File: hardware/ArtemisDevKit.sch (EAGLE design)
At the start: 79 parts, among them J2 CORTEX_JTAG_DEBUG_MINIMUM_PTH, J3 CORTEX_JTAG_DEBUG_PTH, J5 1X04_SMD_STRAIGHT_COMBO, J6 QWIIC_RIGHT_ANGLE, J7 CAMERA-HIMAX, J9 1X04_SMD_STRAIGHT_COMBO, U1 DAPLINK_KL26Z, U2 ARTEMIS_MODULESMD, U3 LIS2DH12, U4 AP2127K-1.8V, X1 16MHz, Y1 32.768kHz

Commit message: apply changes from proto review
- labeled jumpers w/ matching names and description
- labeled accelerometer axes (bottom)
- increaded power trace widths to 24 mil
- removed VUSB current limiting resistor
- increased buzzard label sizes
- added AP2112K 3.3V regulator (disconnected MKL26Z regulator output from 3.3V bus to avoid contention)
- added product name on top silk
- changed reset button to the tall smd version
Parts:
- removed JP1: JUMPER-SMT_2_NC_TRACE_SILK, SparkFun-Jumpers:JUMPER-SMT_2_NC_TRACE_SILK
- removed R17: 10, SparkFun-Resistors:10OHM-0603-1/10W-1%
- removed TP11, TP3, TP4: TEST-POINT3X5, SparkFun-Connectors:TEST-POINT3X5
- added TGT_BOOT: JUMPER-SMT_2_NC_TRACE_SILK, SparkFun-Jumpers:JUMPER-SMT_2_NC_TRACE_SILK
- added U5: 3.3V, SparkFun-IC-Power:V_REG_AP2112K-3.3V
- S2: device SparkFun-Switches:MOMENTARY-SWITCH-SPST-SMD-4.6X2.8MM -> SparkFun-Switches:MOMENTARY-SWITCH-SPST-SMD-5.2MM-TALL
- renumbered JP2 to TGT_SWD_CLK
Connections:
- removed net VBUS_IF: D6.5, J1.VBUS, J12.3, J12.4, J4.3, J4.4, J8.3, J8.4, R17.1
- removed net VBUS_IF2: C12.1, C13.1, R17.2, R19.2, U1.VREGIN
- new net V_USB: C12.1, C13.1, D6.5, J1.VBUS, J12.3, J12.4, J4.3, J4.4, J8.3, J8.4, R19.2, U1.VREGIN, U5.EN, U5.IN
- net !TGT_RST: no longer TP11.1
- net 3.3V: now also U5.OUT; no longer U1.VOUT33
- net GND: now also U5.GND
- net N$18: now also TGT_BOOT.1; no longer JP1.1
- net TGT_BOOT: now also TGT_BOOT.2; no longer JP1.2
- net TGT_RX: no longer TP4.1
- net TGT_TX: no longer TP3.1
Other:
- note added: "Cut to isolate Artemis boot pin from interface chip"
- note added: "Cut to isolate Artemis swd clock from interface chip"

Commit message: update to use MKL26Z128VFM4 from SparkFun library
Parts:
- U1: value DAPLINK_KL26Z -> DAPLINK_KL26Z128VFM4; device ArtemisDevKit:DAPLINK_KL26Z -> SparkFun-IC-Microcontroller:DAPLINK_KL26Z128VFM4

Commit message: update eagle libraries in brd + sch
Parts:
- J12, J8: device SparkFun-Connectors:CONN_08NO_SILK_FEMALE_PTH -> SparkFun-Connectors:CONN_08NO_SILK_DNP
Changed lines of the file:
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@@
 <part name="SUPPLY22" library="SparkFun-PowerSymbols" deviceset="3.3V" device=""/>
 <part name="J4" library="SparkFun-Connectors" deviceset="CONN_08" device="SMD-COMBO-FEMALE"/>
-<part name="J8" library="SparkFun-Connectors" deviceset="CONN_08" device="NO_SILK_FEMALE_PTH"/>
-<part name="J12" library="SparkFun-Connectors" deviceset="CONN_08" device="NO_SILK_FEMALE_PTH"/>
+<part name="J8" library="SparkFun-Connectors" deviceset="CONN_08" device="NO_SILK_DNP"/>
+<part name="J12" library="SparkFun-Connectors" deviceset="CONN_08" device="NO_SILK_DNP"/>
 <part name="SUPPLY5" library="SparkFun-PowerSymbols" deviceset="1.8V" device=""/>
 <part name="J14" library="SparkFun-Connectors" deviceset="CONN_12" device="NO_SILK"/>

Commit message: replace sparkfun logo in schematic
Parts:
- added LOGO2: SFE_LOGO_NAME_FLAME.2_INCH, SparkFun-Aesthetics:SFE_LOGO_NAME_FLAME.2_INCH

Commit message: QC double check changes
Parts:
- J1: value (none) -> USB
- J10, J11: value (none) -> SMD
- J14, J22, J23, J24, J25, J26: value (none) -> PTH
- J5, J9: value 1X04_SMD_STRAIGHT_COMBO -> SMD
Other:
- note added: "power rail intended for output only"
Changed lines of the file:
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@@
 <part name="C4" library="SparkFun-Capacitors" deviceset="0.1UF" device="-0603-25V-5%" value="0.1uF"/>
 <part name="R12" library="SparkFun-Resistors" deviceset="10KOHM" device="-0603-1/10W-1%" value="10k"/>
-<part name="J1" library="SparkFun-Connectors" deviceset="USB_C" device="_2-LAYER"/>
+<part name="J1" library="SparkFun-Connectors" deviceset="USB_C" device="_2-LAYER" value="USB"/>
 <part name="R6" library="SparkFun-Resistors" deviceset="5.1KOHM" device="5.1KOHM-0603-1/10W-1%" value="5.1k"/>
 <part name="R7" library="SparkFun-Resistors" deviceset="5.1KOHM" device="5.1KOHM-0603-1/10W-1%" value="5.1k"/>
@@
 <part name="J12" library="SparkFun-Connectors" deviceset="CONN_08" device="NO_SILK_DNP"/>
 <part name="SUPPLY5" library="SparkFun-PowerSymbols" deviceset="1.8V" device=""/>
-<part name="J14" library="SparkFun-Connectors" deviceset="CONN_12" device="NO_SILK"/>
-<part name="J22" library="SparkFun-Connectors" deviceset="CONN_12" device="NO_SILK"/>
-<part name="J23" library="SparkFun-Connectors" deviceset="CONN_12" device="NO_SILK"/>
-<part name="J24" library="SparkFun-Connectors" deviceset="CONN_12" device="NO_SILK"/>
-<part name="J25" library="SparkFun-Connectors" deviceset="CONN_12" device="NO_SILK"/>
-<part name="J26" library="SparkFun-Connectors" deviceset="CONN_12" device="NO_SILK"/>
+<part name="J14" library="SparkFun-Connectors" deviceset="CONN_12" device="NO_SILK" value="PTH"/>
+<part name="J22" library="SparkFun-Connectors" deviceset="CONN_12" device="NO_SILK" value="PTH"/>
+<part name="J23" library="SparkFun-Connectors" deviceset="CONN_12" device="NO_SILK" value="PTH"/>
+<part name="J24" library="SparkFun-Connectors" deviceset="CONN_12" device="NO_SILK" value="PTH"/>
+<part name="J25" library="SparkFun-Connectors" deviceset="CONN_12" device="NO_SILK" value="PTH"/>
+<part name="J26" library="SparkFun-Connectors" deviceset="CONN_12" device="NO_SILK" value="PTH"/>
 <part name="GND1" library="SparkFun-PowerSymbols" deviceset="GND" device=""/>
-<part name="J5" library="SparkFun-Connectors" deviceset="CONN_04" device="SMD_STRAIGHT_COMBO" value="1X04_SMD_STRAIGHT_COMBO"/>
-<part name="J9" library="SparkFun-Connectors" deviceset="CONN_04" device="SMD_STRAIGHT_COMBO" value="1X04_SMD_STRAIGHT_COMBO"/>
-<part name="J10" library="SparkFun-Connectors" deviceset="CONN_08" device="SMD-COMBO-FEMALE"/>
-<part name="J11" library="SparkFun-Connectors" deviceset="CONN_08" device="SMD-COMBO-FEMALE"/>
+<part name="J5" library="SparkFun-Connectors" deviceset="CONN_04" device="SMD_STRAIGHT_COMBO" value="SMD"/>
+<part name="J9" library="SparkFun-Connectors" deviceset="CONN_04" device="SMD_STRAIGHT_COMBO" value="SMD"/>
+<part name="J10" library="SparkFun-Connectors" deviceset="CONN_08" device="SMD-COMBO-FEMALE" value="SMD"/>
+<part name="J11" library="SparkFun-Connectors" deviceset="CONN_08" device="SMD-COMBO-FEMALE" value="SMD"/>
 <part name="GND23" library="SparkFun-PowerSymbols" deviceset="GND" device=""/>
 <part name="TGT_BOOT" library="SparkFun-Jumpers" deviceset="JUMPER-SMT_2_NC_TRACE" device="_SILK" package3d_urn="urn:adsk.eagle:package:39281/1"/>
@@
 <text x="116.84" y="203.2" size="1.27" layer="97" font="vector">Cut to isolate Artemis swd
 clock  from interface chip</text>
+<text x="363.22" y="180.34" size="1.778" layer="97" font="vector">power rail intended for output only</text>
 </plain>
 <instances>

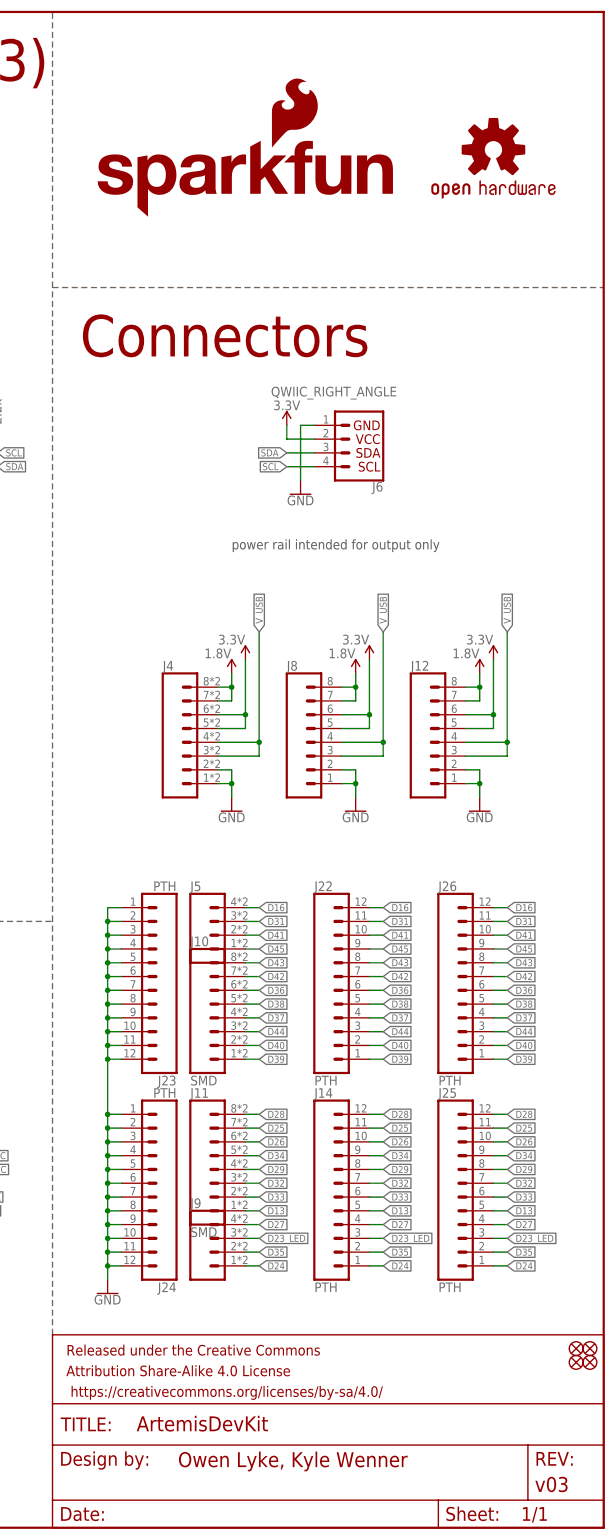
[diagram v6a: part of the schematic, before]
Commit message: address Pete's reviews
- improve GND pour on lower layer
- fix ERC errors (mismatched values, footprints)
- add LED buzzard labels
- fix version in copper and schematic
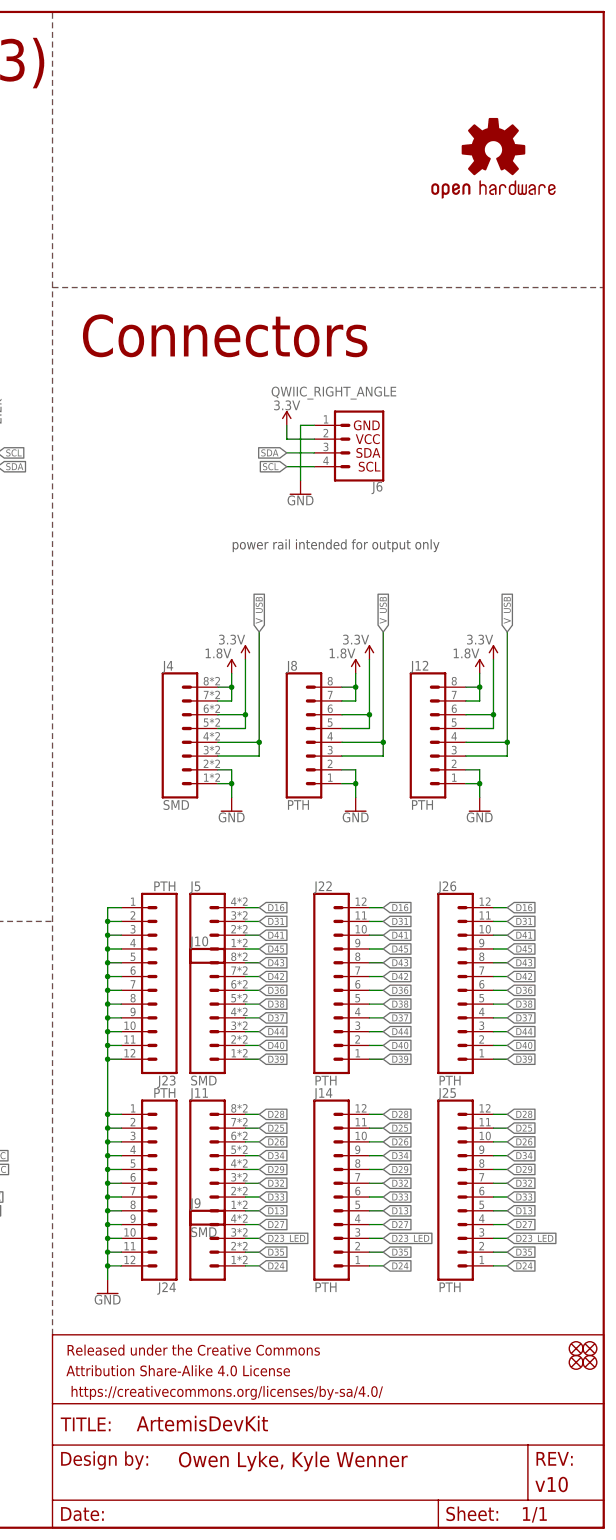
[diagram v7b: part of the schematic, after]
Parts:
- removed LOGO2: SFE_LOGO_NAME_FLAME.2_INCH, SparkFun-Aesthetics:SFE_LOGO_NAME_FLAME.2_INCH
- FRAME1: REV v03 -> v10
- J12, J8: value (none) -> PTH
- J4: value (none) -> SMD

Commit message: update silkscreen
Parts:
- added LOGO2: SFE_LOGO_NAME_FLAME.2_INCH, SparkFun-Aesthetics:SFE_LOGO_NAME_FLAME.2_INCH
- J5, J9: value SMD -> 1X04_SMD_STRAIGHT_COMBO
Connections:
- net CAMERA_D1: now also U2.(SLSDO/SLSDA)D1; no longer U2.(SLMOSI/SLSDA)D1
- net CAMERA_D2: now also U2.(SLSDI)D2; no longer U2.(SLMISO)D2
- net CAMERA_D6: now also U2.(SDA0/SDI0/I2SDAT)~D6; no longer U2.(SDA0/MISO0/I2SDAT)~D6
- net CAMERA_D7: now also U2.(SDO0/CLKOUT)~D7; no longer U2.(MOSI0/CLKOUT)~D7
- net CAMERA_INT: now also U2.(SDO1/TX1/PDMCLK)D10; no longer U2.(MOSI1/TX1/PDMCLK)D10
- net D25: now also U2.(SDA2/SDI2/RX1)~D25; no longer U2.(SDA2/MISO2/RX1)~D25
- net D28: now also U2.(SDO2/I2SWCLK)~D28; no longer U2.(MOSI2/I2SWCLK)~D28
- net D38: now also U2.(SDO3/RX1)D38; no longer U2.(MOSI3/RX1)D38
- net D40: now also U2.(SDA4/SDI4/RX1)D40; no longer U2.(SDA4/MISO4/RX1)D40
- net D43: now also U2.(SDA3/SDI3/RX1)~D43; no longer U2.(SDA3/MISO3/RX1)~D43
- net D44: now also U2.(SDO4)~D44; no longer U2.(MOSI4)~D44
- net SDA: now also U2.(SDA1/SDI1/RX1/SCCIO)D9; no longer U2.(SDA1/MISO1/RX1/SCCIO)D9
- net TGT_BOOT: now also U2.~BOOT(SDO5/RX1/32KHZ); no longer U2.~BOOT(MOSI5/RX1/32KHZ)
- net TGT_RX: now also U2.~D49(RX0/SDA5/SDI5); no longer U2.~D49(RX0/SDA5/MISO5)
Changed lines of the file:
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@@
 <part name="J26" library="SparkFun-Connectors" deviceset="CONN_12" device="NO_SILK" value="PTH"/>
 <part name="GND1" library="SparkFun-PowerSymbols" deviceset="GND" device=""/>
-<part name="J5" library="SparkFun-Connectors" deviceset="CONN_04" device="SMD_STRAIGHT_COMBO" value="SMD"/>
-<part name="J9" library="SparkFun-Connectors" deviceset="CONN_04" device="SMD_STRAIGHT_COMBO" value="SMD"/>
+<part name="J5" library="SparkFun-Connectors" deviceset="CONN_04" device="SMD_STRAIGHT_COMBO" value="1X04_SMD_STRAIGHT_COMBO"/>
+<part name="J9" library="SparkFun-Connectors" deviceset="CONN_04" device="SMD_STRAIGHT_COMBO" value="1X04_SMD_STRAIGHT_COMBO"/>
 <part name="J10" library="SparkFun-Connectors" deviceset="CONN_08" device="SMD-COMBO-FEMALE" value="SMD"/>
 <part name="J11" library="SparkFun-Connectors" deviceset="CONN_08" device="SMD-COMBO-FEMALE" value="SMD"/>
@@
 <part name="SUPPLY30" library="SparkFun-PowerSymbols" deviceset="3.3V" device=""/>
 <part name="SUPPLY29" library="SparkFun-PowerSymbols" deviceset="V_USB" device=""/>
-<part name="SUPPLY31" library="SparkFun-PowerSymbols" deviceset="V_USB" device=""/>
 <part name="U1" library="SparkFun-IC-Microcontroller" deviceset="DAPLINK_KL26Z128VFM4" device=""/>
+<part name="LOGO2" library="SparkFun-Aesthetics" deviceset="SFE_LOGO_NAME_FLAME" device=".2_INCH"/>
 </parts>
 <sheets>
@@
 <wire x1="330.2" y1="35.56" x2="330.2" y2="111.76" width="0.2032" layer="97" style="longdash"/>
 <wire x1="330.2" y1="228.6" x2="431.8" y2="228.6" width="0.2032" layer="97" style="longdash"/>
-<text x="5.08" y="266.7" size="7.62" layer="94" font="vector">Interface MCU - MKL26Z</text>
-<text x="170.18" y="266.7" size="7.62" layer="94" font="vector">Target - Artemis Module (Apollo3)</text>
-<text x="335.28" y="215.9" size="7.62" layer="94" font="vector">Connectors</text>
-<text x="5.08" y="99.06" size="7.62" layer="94" font="vector">USB</text>
-<text x="170.18" y="99.06" size="7.62" layer="94" font="vector">Sensors</text>
+<text x="2.54" y="274.32" size="2.54" layer="94" font="vector">Interface MCU - MKL26Z</text>
+<text x="165.1" y="274.32" size="2.54" layer="94" font="vector">Target - Artemis Module (Apollo3)</text>
+<text x="332.74" y="223.52" size="2.54" layer="94" font="vector">Connectors</text>
+<text x="2.54" y="106.68" size="2.54" layer="94" font="vector">USB</text>
+<text x="165.1" y="106.68" size="2.54" layer="94" font="vector">Sensors</text>
 <text x="65.278" y="141.224" size="1.27" layer="97" font="vector">Cut to isolate Artemis boot
 pin from interface chip</text>
@@
 </instance>
 <instance part="J9" gate="J1" x="360.68" y="50.8" smashed="yes">
-<attribute name="NAME" x="355.6" y="58.928" size="1.778" layer="95" font="vector"/>
+<attribute name="NAME" x="363.22" y="43.688" size="1.778" layer="95" font="vector"/>
 </instance>
 <instance part="J10" gate="G$1" x="360.68" y="93.98" smashed="yes">
 <attribute name="VALUE" x="355.6" y="81.534" size="1.778" layer="96" font="vector"/>
-<attribute name="NAME" x="355.6" y="107.188" size="1.778" layer="95" font="vector"/>
+<attribute name="NAME" x="363.22" y="81.788" size="1.778" layer="95" font="vector"/>
 </instance>
 <instance part="J11" gate="G$1" x="360.68" y="66.04" smashed="yes">
-<attribute name="VALUE" x="355.6" y="53.594" size="1.778" layer="96" font="vector"/>
+<attribute name="VALUE" x="355.6" y="43.434" size="1.778" layer="96" font="vector"/>
 <attribute name="NAME" x="355.6" y="79.248" size="1.778" layer="95" font="vector"/>
 </instance>
@@
 <attribute name="VALUE" x="10.16" y="239.014" size="1.778" layer="96" align="bottom-center"/>
 </instance>
-<instance part="SUPPLY31" gate="G$1" x="152.4" y="71.12" smashed="yes">
-<attribute name="VALUE" x="152.4" y="73.914" size="1.778" layer="96" align="bottom-center"/>
-</instance>
 <instance part="U1" gate="G$1" x="88.9" y="187.96" smashed="yes"/>
+<instance part="LOGO2" gate="G$1" x="337.82" y="241.3" smashed="yes"/>
 </instances>
 <busses>
@@
 </segment>
 <segment>
-<pinref part="U2" gate="U1" pin="~D49(RX0/SDA5/MISO5)"/>
+<pinref part="U2" gate="U1" pin="~D49(RX0/SDA5/SDI5)"/>
 <wire x1="218.44" y1="198.12" x2="220.98" y2="198.12" width="0.1524" layer="91"/>
 <label x="218.44" y="198.12" size="1.27" layer="95" font="vector" rot="R180" xref="yes"/>
@@
 <wire x1="317.5" y1="200.66" x2="317.5" y2="195.58" width="0.1524" layer="91"/>
 <junction x="317.5" y="195.58"/>
-<pinref part="U2" gate="U1" pin="(SDA1/MISO1/RX1/SCCIO)D9"/>
+<pinref part="U2" gate="U1" pin="(SDA1/SDI1/RX1/SCCIO)D9"/>
 </segment>
 <segment>
@@
 </segment>
 <segment>
-<pinref part="U2" gate="U1" pin="(SLMOSI/SLSDA)D1"/>
+<pinref part="U2" gate="U1" pin="(SLSDO/SLSDA)D1"/>
 <wire x1="292.1" y1="215.9" x2="289.56" y2="215.9" width="0.1524" layer="91"/>
 <label x="292.1" y="215.9" size="1.27" layer="95" font="vector" xref="yes"/>
@@
 </segment>
 <segment>
-<pinref part="U2" gate="U1" pin="(SDA0/MISO0/I2SDAT)~D6"/>
+<pinref part="U2" gate="U1" pin="(SDA0/SDI0/I2SDAT)~D6"/>
 <wire x1="289.56" y1="203.2" x2="292.1" y2="203.2" width="0.1524" layer="91"/>
 <label x="292.1" y="203.2" size="1.27" layer="95" font="vector" xref="yes"/>
@@
 </segment>
 <segment>
-<pinref part="U2" gate="U1" pin="(MOSI0/CLKOUT)~D7"/>
+<pinref part="U2" gate="U1" pin="(SDO0/CLKOUT)~D7"/>
 <wire x1="292.1" y1="200.66" x2="289.56" y2="200.66" width="0.1524" layer="91"/>
 <label x="292.1" y="200.66" size="1.27" layer="95" font="vector" xref="yes"/>
@@
 </segment>
 <segment>
-<pinref part="U2" gate="U1" pin="(SLMISO)D2"/>
+<pinref part="U2" gate="U1" pin="(SLSDI)D2"/>
 <wire x1="292.1" y1="213.36" x2="289.56" y2="213.36" width="0.1524" layer="91"/>
 <label x="292.1" y="213.36" size="1.27" layer="95" font="vector" xref="yes"/>
@@
 <wire x1="289.56" y1="193.04" x2="292.1" y2="193.04" width="0.1524" layer="91"/>
 <label x="292.1" y="193.04" size="1.27" layer="95" font="vector" xref="yes"/>
-<pinref part="U2" gate="U1" pin="(MOSI1/TX1/PDMCLK)D10"/>
+<pinref part="U2" gate="U1" pin="(SDO1/TX1/PDMCLK)D10"/>
 </segment>
 </net>
@@
 <net name="D44" class="0">
 <segment>
-<pinref part="U2" gate="U1" pin="(MOSI4)~D44"/>
+<pinref part="U2" gate="U1" pin="(SDO4)~D44"/>
 <wire x1="292.1" y1="139.7" x2="289.56" y2="139.7" width="0.1524" layer="91"/>
 <label x="292.1" y="139.7" size="1.27" layer="95" font="vector" xref="yes"/>
@@
 <net name="D40" class="0">
 <segment>
-<pinref part="U2" gate="U1" pin="(SDA4/MISO4/RX1)D40"/>
+<pinref part="U2" gate="U1" pin="(SDA4/SDI4/RX1)D40"/>
 <wire x1="292.1" y1="149.86" x2="289.56" y2="149.86" width="0.1524" layer="91"/>
 <label x="292.1" y="149.86" size="1.27" layer="95" font="vector" xref="yes"/>
@@
 <net name="D38" class="0">
 <segment>
-<pinref part="U2" gate="U1" pin="(MOSI3/RX1)D38"/>
+<pinref part="U2" gate="U1" pin="(SDO3/RX1)D38"/>
 <wire x1="292.1" y1="154.94" x2="289.56" y2="154.94" width="0.1524" layer="91"/>
 <label x="292.1" y="154.94" size="1.27" layer="95" font="vector" xref="yes"/>
@@
 <net name="D43" class="0">
 <segment>
-<pinref part="U2" gate="U1" pin="(SDA3/MISO3/RX1)~D43"/>
+<pinref part="U2" gate="U1" pin="(SDA3/SDI3/RX1)~D43"/>
 <wire x1="292.1" y1="142.24" x2="289.56" y2="142.24" width="0.1524" layer="91"/>
 <label x="292.1" y="142.24" size="1.27" layer="95" font="vector" xref="yes"/>
@@
 <net name="D25" class="0">
 <segment>
-<pinref part="U2" gate="U1" pin="(SDA2/MISO2/RX1)~D25"/>
+<pinref part="U2" gate="U1" pin="(SDA2/SDI2/RX1)~D25"/>
 <wire x1="292.1" y1="170.18" x2="289.56" y2="170.18" width="0.1524" layer="91"/>
 <label x="292.1" y="170.18" size="1.27" layer="95" font="vector" xref="yes"/>
@@
 <net name="D28" class="0">
 <segment>
-<pinref part="U2" gate="U1" pin="(MOSI2/I2SWCLK)~D28"/>
+<pinref part="U2" gate="U1" pin="(SDO2/I2SWCLK)~D28"/>
 <wire x1="292.1" y1="162.56" x2="289.56" y2="162.56" width="0.1524" layer="91"/>
 <label x="292.1" y="162.56" size="1.27" layer="95" font="vector" xref="yes"/>
@@
 <net name="TGT_BOOT" class="0">
 <segment>
-<pinref part="U2" gate="U1" pin="~BOOT(MOSI5/RX1/32KHZ)"/>
+<pinref part="U2" gate="U1" pin="~BOOT(SDO5/RX1/32KHZ)"/>
 <wire x1="200.66" y1="208.28" x2="203.2" y2="208.28" width="0.1524" layer="91"/>
 <label x="200.66" y="208.28" size="1.27" layer="95" font="vector" rot="R180" xref="yes"/>
@@
 <segment>
 <pinref part="D6" gate="D1" pin="5"/>
-<wire x1="99.06" y1="68.58" x2="96.52" y2="68.58" width="0.1524" layer="91"/>
-<wire x1="99.06" y1="68.58" x2="99.06" y2="76.2" width="0.1524" layer="91"/>
-<junction x="99.06" y="68.58"/>
-<label x="99.06" y="76.2" size="1.27" layer="95" font="vector" rot="R90" xref="yes"/>
 <pinref part="R19" gate="G$1" pin="2"/>
 <wire x1="137.16" y1="68.58" x2="127" y2="68.58" width="0.1524" layer="91"/>
@@
 <wire x1="119.38" y1="68.58" x2="127" y2="68.58" width="0.1524" layer="91"/>
 <junction x="127" y="68.58"/>
-<wire x1="99.06" y1="68.58" x2="114.3" y2="68.58" width="0.1524" layer="91"/>
-</segment>
-<segment>
+<wire x1="96.52" y1="68.58" x2="114.3" y2="68.58" width="0.1524" layer="91"/>
+</segment>
+<segment>
